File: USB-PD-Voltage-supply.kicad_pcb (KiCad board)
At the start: 2 copper layers, 79.1 x 78.8 mm, 221 parts, among them J1 DC-005-5A-2.5-SMT, J2 Conn_01x07_Pin, J3 Conn_01x04_Pin, J4 TYPE-C-31-M-31, J5 Conn_01x11_Pin, J6 Conn_01x11_Pin, J7 Conn_01x11_Pin, Q1 STL6P3LLH6, Q2 STL6P3LLH6, SW1 TS-1088-AR02016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

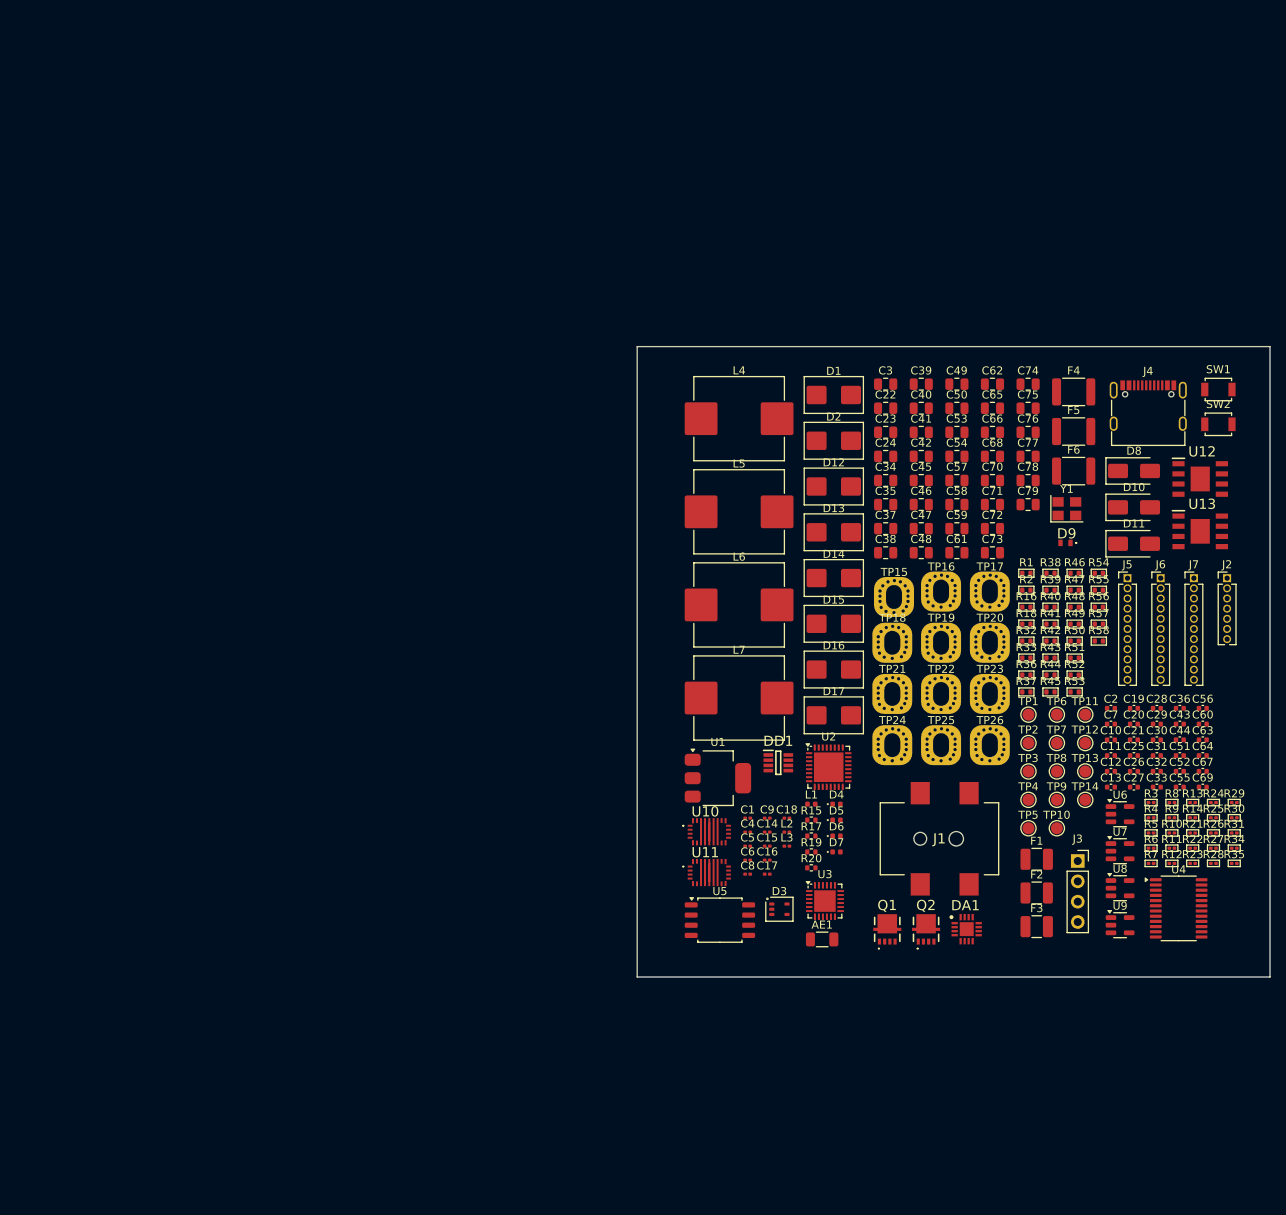
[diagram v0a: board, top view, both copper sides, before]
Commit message: Added JLCPCB BOM + placed main components on PCB to form a prototype
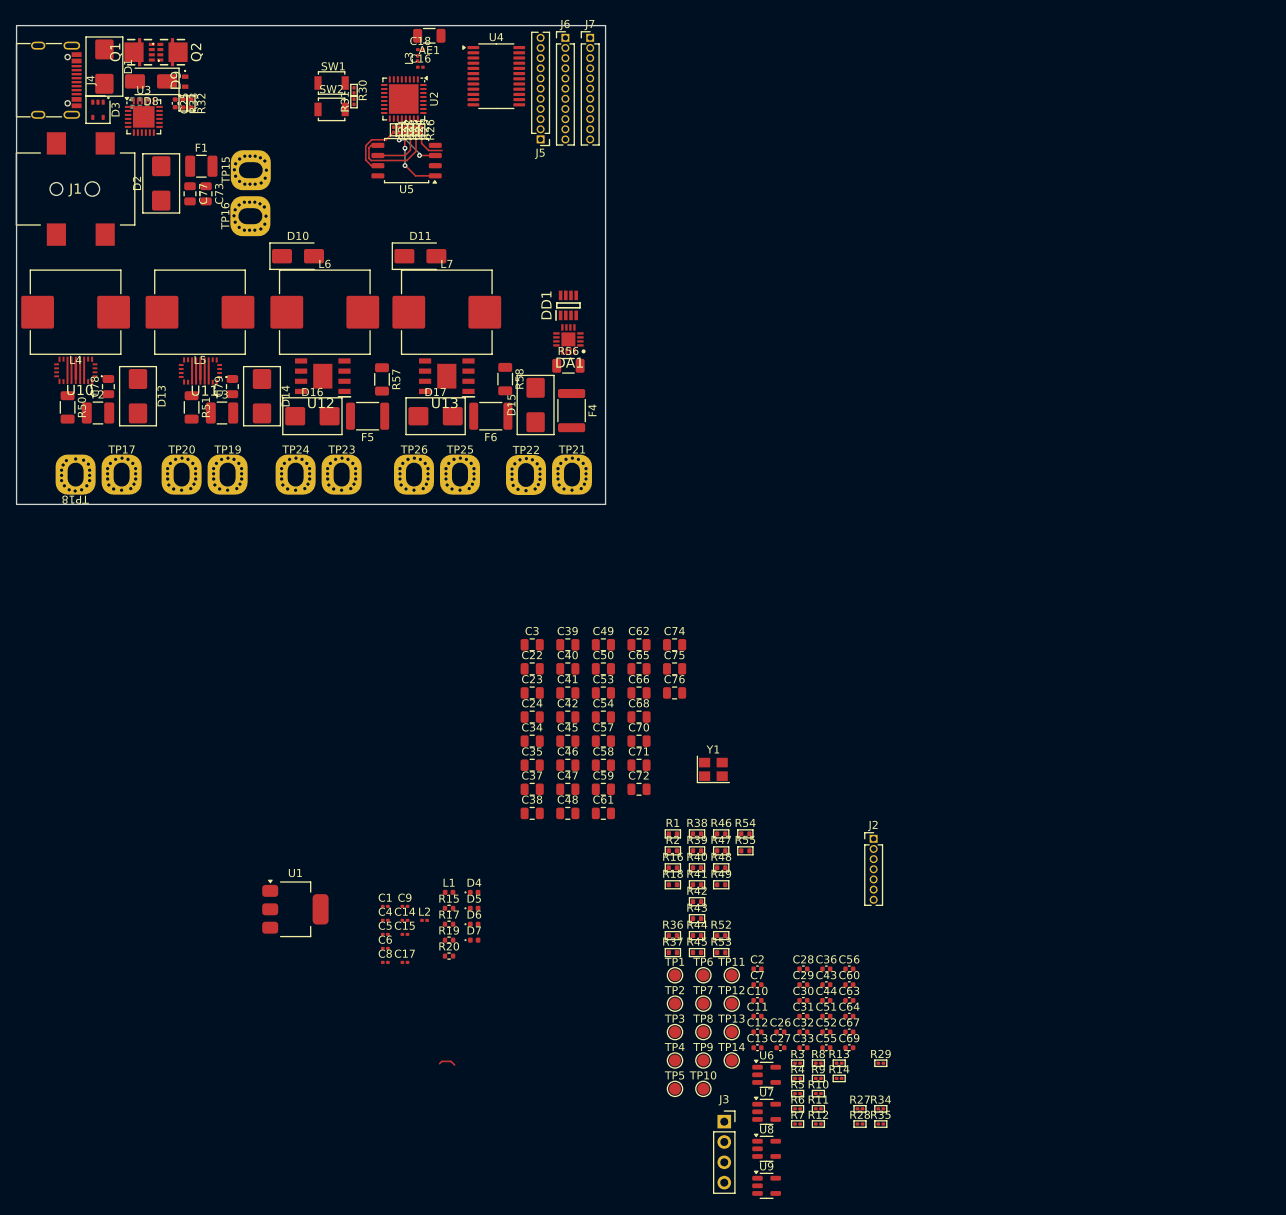
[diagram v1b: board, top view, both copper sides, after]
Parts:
- removed D12: SMBJ40CA, PCM_Diode_SMD_AKL:D_SMB_TVS
- C19, C20, C21: moved to B.Cu
- R50, R51, R56, R57, R58: footprint PCM_Resistor_SMD_AKL:R_0402_1005Metric -> Resistor_SMD:R_1206_3216Metric
- moved C21 148.4 mm to (1983.8, -46.4), turned to -90 degrees
- moved C20 145.7 mm to (1985.7, -46.4), turned to -90 degrees
- moved C19 145.5 mm to (1984.7, -46.4), turned to -90 degrees
- moved C25 144.9 mm to (1989.2, -46.3), turned to -90 degrees
- moved Q2 144.6 mm to (1988.8, -52.7), turned to -90 degrees
- moved Q1 144.1 mm to (1984.7, -52.7), turned to 90 degrees
- moved J4 143.9 mm to (1973.1, -49.2), turned to -90 degrees
- moved R31 143.0 mm to (2011.5, -46.5), turned to 90 degrees
- moved R30 142.7 mm to (2011.5, -47.9), turned to -90 degrees
- moved F1 135.7 mm to (1992.4, -38.4)
- moved J1 135.1 mm to (1976.7, -35.6)
- moved R23 134.6 mm to (2017.8, -43.0), turned to -90 degrees
- moved U4 134.5 mm to (2029.3, -49.7)
- moved R22 133.8 mm to (2017.2, -43.0), turned to -90 degrees
- moved R21 133.1 mm to (2016.5, -43.0), turned to -90 degrees
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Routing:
- net SPID: track 0.00 -> 11.4 mm
- net SPICS0: track 0.00 -> 8.48 mm, vias 0 -> 2
- net SPIHD: track 0.00 -> 7.77 mm
- net SPIQ: track 0.00 -> 7.17 mm
- net SPICLK: track 0.00 -> 6.57 mm
- net SPIWP: track 0.00 -> 6.42 mm, vias 0 -> 2
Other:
- board size 79.1 x 78.8 mm -> 73.6 x 59.8 mm

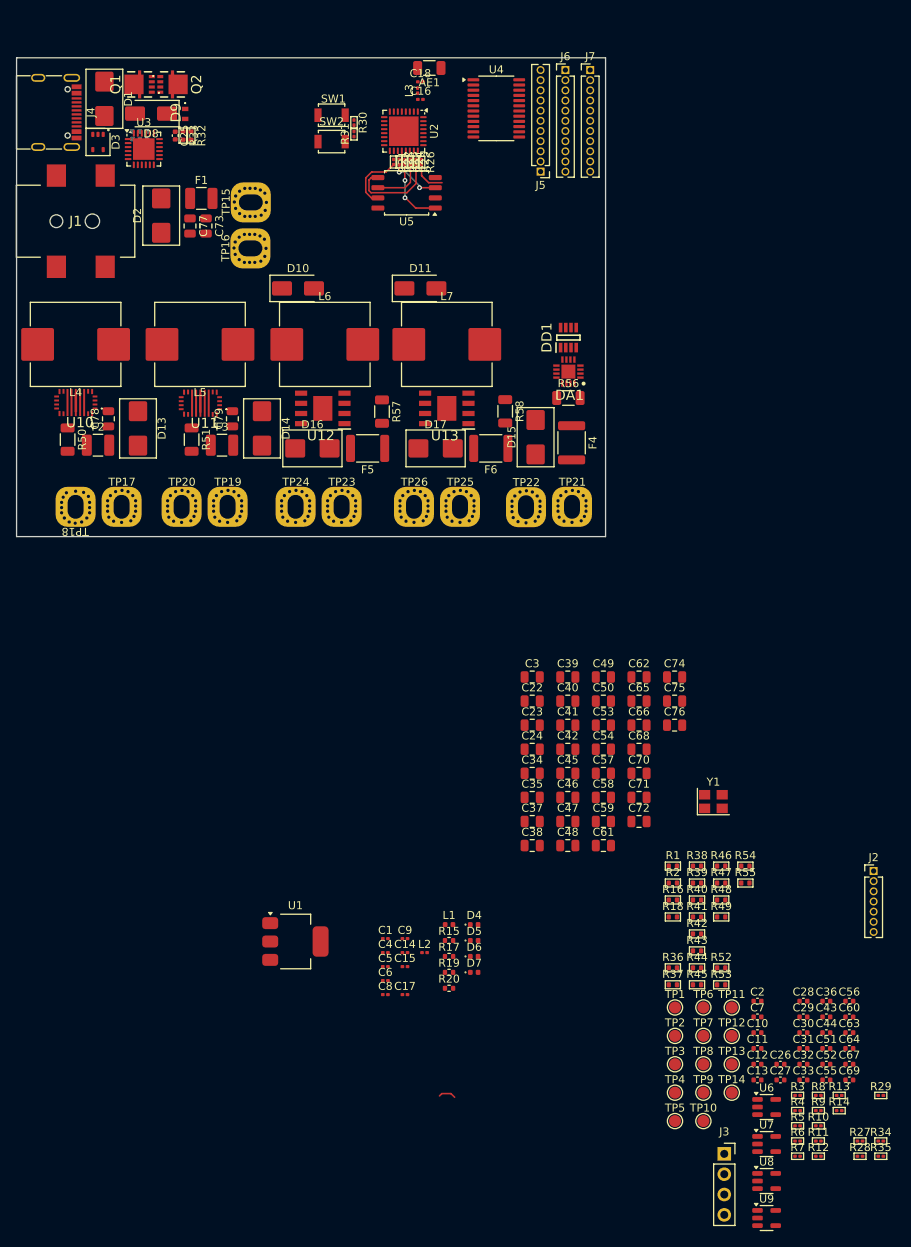
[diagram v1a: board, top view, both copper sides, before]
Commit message: Finished components placement + silkscreen placement Reviewed schematics, changed outline Ready for tracing
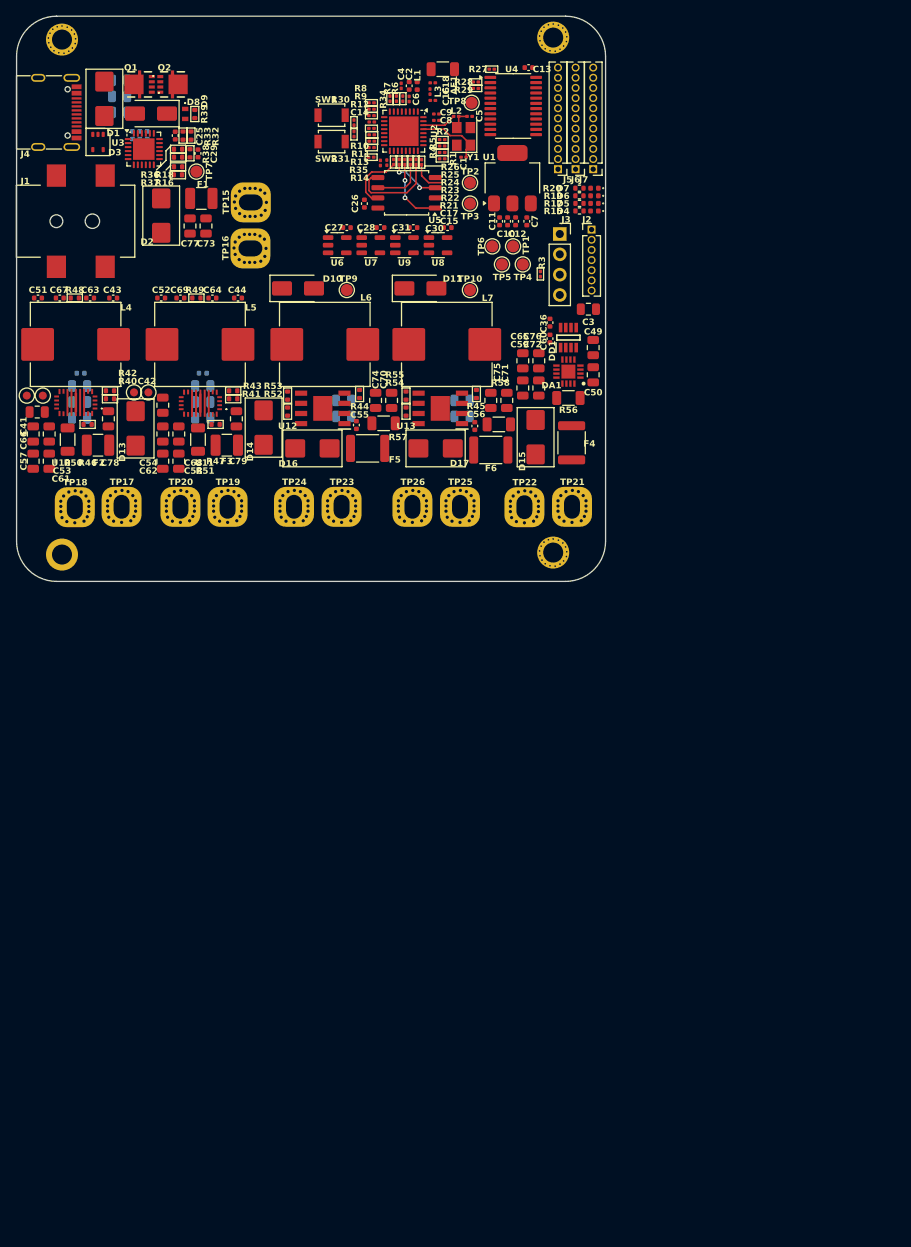
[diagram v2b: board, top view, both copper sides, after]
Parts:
- added ?: , , F.Cu at (2036.4, 5.82)
- added ?: , , F.Cu at (1975.0, -58.3)
- added ?: , , F.Cu at (1975.0, 6.07)
- added ?: , , F.Cu at (2036.4, -58.5)
- C22, C23, C24, C32, C33, C34, C35, C37, C38, C39, C40, C45, C46, C47, C48: moved to B.Cu
- C67, C69: value 2.4nF -> 2.2nF
- R1, R2: footprint PCM_Resistor_SMD_AKL:R_0402_1005Metric -> PCM_Resistor_SMD_AKL:R_0201_0603Metric
- R48, R49: value 70.6K -> 71.5K
- moved R34 144.0 mm to (2016.0, -50.9), turned to 90 degrees
- moved R28 142.6 mm to (2026.7, -53.0)
- moved R27 141.7 mm to (2028.7, -54.6)
- moved R12 141.6 mm to (2013.7, -48.8)
- moved R7 141.4 mm to (2016.8, -50.9), turned to -90 degrees
- moved R35 141.2 mm to (2013.7, -44.8), turned to 180 degrees
- moved R6 139.3 mm to (2017.6, -50.9), turned to -90 degrees
- moved R11 137.6 mm to (2013.7, -46.4)
- moved C67 137.5 mm to (1974.7, -26.0), turned to 180 degrees
- moved R9 137.1 mm to (2013.7, -49.6)
- moved R10 136.6 mm to (2013.7, -47.2)
- moved R8 136.1 mm to (2013.7, -50.4)
- moved C51 136.1 mm to (1972.0, -26.0)
- moved R29 135.7 mm to (2026.7, -52.2)
- moved R13 132.8 mm to (2013.7, -45.6)
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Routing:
- net Net-(U2-XTAL_N): track 0.00 -> 8.48 mm
- net Net-(U2-XTAL_P): track 0.00 -> 4.23 mm
- net Net-(C5-Pad1): track 0.00 -> 2.54 mm
- net SPIQ: track 7.17 -> 4.97 mm
- net Earth: vias 0 -> 51
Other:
- board size 73.6 x 59.8 mm -> 73.6 x 70.6 mm

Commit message: power poligons partly done
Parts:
- moved TP7 18.6 mm to (1980.4, -56.5)
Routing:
- net PD-Voltage: vias 0 -> 40
- net Net-(D11-K): vias 0 -> 46
- net Net-(D10-K): vias 0 -> 42
- net Net-(C70-Pad1): vias 0 -> 45
- net Earth: vias 51 -> 65
- net +5.2V_USB_: vias 0 -> 43
- added copper zone on F.Cu, net +5.2V
- added copper zone on F.Cu, net +5.2V_USB
- added copper zone on B.Cu, net +5.2V_USB_
- added copper zone on F.Cu, net +5.2V_USB_
- added copper zone on F.Cu, net +5V_USB
- added copper zone on F.Cu, net Earth
- added copper zone on B.Cu, net Net-(C70-Pad1)
- added copper zone on F.Cu, net Net-(C70-Pad1)
- added copper zone on B.Cu, net Net-(D10-K)
- added copper zone on F.Cu, net Net-(D10-K)
- added copper zone on B.Cu, net Net-(D11-K)
- added copper zone on F.Cu, net Net-(D11-K)
- added copper zone on F.Cu, net Net-(D13-A)
- added copper zone on F.Cu, net Net-(D14-A)
- added copper zone on F.Cu, net Net-(D15-A)
- added copper zone on F.Cu, net Net-(D16-A)
- added copper zone on F.Cu, net Net-(D17-A)
- added copper zone on F.Cu, net Net-(F1-Pad2)
- added copper zone on F.Cu, net Net-(U10-SW1)
- added copper zone on F.Cu, net Net-(U10-SW2)
- added copper zone on F.Cu, net Net-(U11-SW1)
- added copper zone on F.Cu, net Net-(U11-SW2)
- added copper zone on F.Cu, net PD-Voltage
- added copper zone on F.Cu, net PD_VDD
- added copper zone on F.Cu, net VOUT1
- added copper zone on F.Cu, net VOUT1_
- added copper zone on F.Cu, net VOUT2
- added copper zone on F.Cu, net VOUT2_
- added copper zone on F.Cu, net VOUT3
- added copper zone on F.Cu, net VOUT3_

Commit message: Finished rev0
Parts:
- added G***: LOGO, LOGO, F.Cu at (150.8, 78.4)
- added G***: LOGO, LOGO, B.Cu at (136.7, 94.6)
- added G***: LOGO, LOGO, B.Cu at (135.4, 109.7)
- added G***: LOGO, LOGO, B.Cu at (133.5, 101.7)
- added G***: LOGO, LOGO, B.Cu at (134.5, 93.9)
- added G***: LOGO, LOGO, B.Cu at (163.8, 86.1)
- added kibuzzard-689E2C41: G***, kibuzzard-689E2C41, F.Cu at (149.8, 68.5)
- moved TP13 1855.7 mm to (134.2, 109.6)
- moved R47 1853.9 mm to (144.4, 113.7)
- moved ? 1853.9 mm to (186.6, 129.6)
- moved ? 1853.9 mm to (186.6, 65.2)
- moved C2 1853.9 mm to (168.6, 71.3)
- moved C20 1853.9 mm to (135.8, 77.5)
- moved C25 1853.9 mm to (139.3, 77.5)
- moved C31 1853.9 mm to (169.1, 89.0)
- moved C4 1853.9 mm to (167.6, 71.3)
- moved C41 1853.9 mm to (122.1, 112.1)
- moved C43 1853.9 mm to (131.6, 97.8)
- moved C49 1853.9 mm to (191.6, 104.0)
- moved C50 1853.9 mm to (191.6, 107.4)
- moved C52 1853.9 mm to (137.6, 97.8)
- moved C53 1853.9 mm to (123.6, 114.8)
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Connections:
- U4 pad 10: BUTTON_2 -> TPS2_EN
- U4 pad 11: BUTTON_3 -> TPS1_EN
- U4 pad 4: TPS1_EN -> BUTTON_3
- U4 pad 5: TPS2_EN -> BUTTON_2
- U4 pad 6: PD-RST -> BUTTON_1
- U4 pad 7: LDO_EN -> ST7789_RST
- U4 pad 8: ST7789_RST -> LDO_EN
- U4 pad 9: BUTTON_1 -> PD-RST
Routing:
- net SCL: track 0.00 -> 115.4 mm, vias 0 -> 6
- net SDA: track 0.00 -> 112.5 mm, vias 0 -> 8
- net TPS1_EN: track 0.00 -> 84.0 mm, vias 0 -> 3
- net +5V_USB: track 0.00 -> 74.6 mm, vias 0 -> 24
- net VOUT1: track 0.00 -> 62.1 mm, vias 0 -> 3
- net SPI_SCLK: track 0.00 -> 61.2 mm, vias 0 -> 3
- net SPI_MOSI: track 0.00 -> 58.8 mm, vias 0 -> 3
- net PD-RST: track 0.00 -> 56.6 mm, vias 0 -> 2
- net TPS2_EN: track 0.00 -> 56.1 mm, vias 0 -> 2
- net POT_CS: track 0.00 -> 55.8 mm, vias 0 -> 2
- net PD-Voltage: track 0.00 -> 54.6 mm, vias 40 -> 172
- net +3.3V_LDO: track 0.00 -> 49.2 mm, vias 0 -> 14
- net VOUT2: track 0.00 -> 48.9 mm, vias 0 -> 3
- net LDO_EN: track 0.00 -> 44.5 mm, vias 0 -> 2
- net VOUT1_: track 0.00 -> 43.6 mm, vias 0 -> 3
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- added copper zone on F.Cu, net +3.3V_LDO
- added copper zone on In2.Cu, net +3.3V_LDO
- added copper zone on In2.Cu, net +5.2V
- added copper zone on B.Cu, net +5V_USB
- added copper zone on B.Cu, net Earth
- added copper zone on In1.Cu, net Earth
- added copper zone on In2.Cu, net Earth
- added copper zone on In2.Cu, net PD-Voltage
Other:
- outline, holes or cut-outs redrawn
- copper layers 2 -> 4
- board text added: "( PD or DC-Jack )"
- board text added: "0.5"
- board text added: "0.8"
- board text added: "1"
- board text added: "2"
- board text added: "22"
- board text added: "3"
- board text added: "3A"
- board text added: "4"
- board text added: "5"
- board text added: "5.0"
- board text added: "5.1"
- board text added: "5.3"
- board text added: "6A"
- board text added: "Current"
- board text added: "DC 12-21V"
- board text added: "Find peace within the chaos of life"
- board text added: "Out"
- board text added: "Out 1"
- board text added: "Out 2"
- board text added: "Out 3"
- board text added: "Out 4"
- board text added: "Out 5"
- board text added: "USB-PD Voltage supply"
- board text added: "Vin"
- board text added: "Vmax"
- board text added: "Vmin"
- board text added: "https://github.com/Madjogger1202/USB-PD-Voltage-supply"
